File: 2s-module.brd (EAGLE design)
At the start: 19.4 x 48.2 mm, 36 parts, among them J1 CQ-USB-C16PSMT01, Q1 IRFR9020A, U1 MCP4725, U2 PC817XI, U3 LM393DR, U4 MICROCHIP_MIC5219-3_3YM5-TRMI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

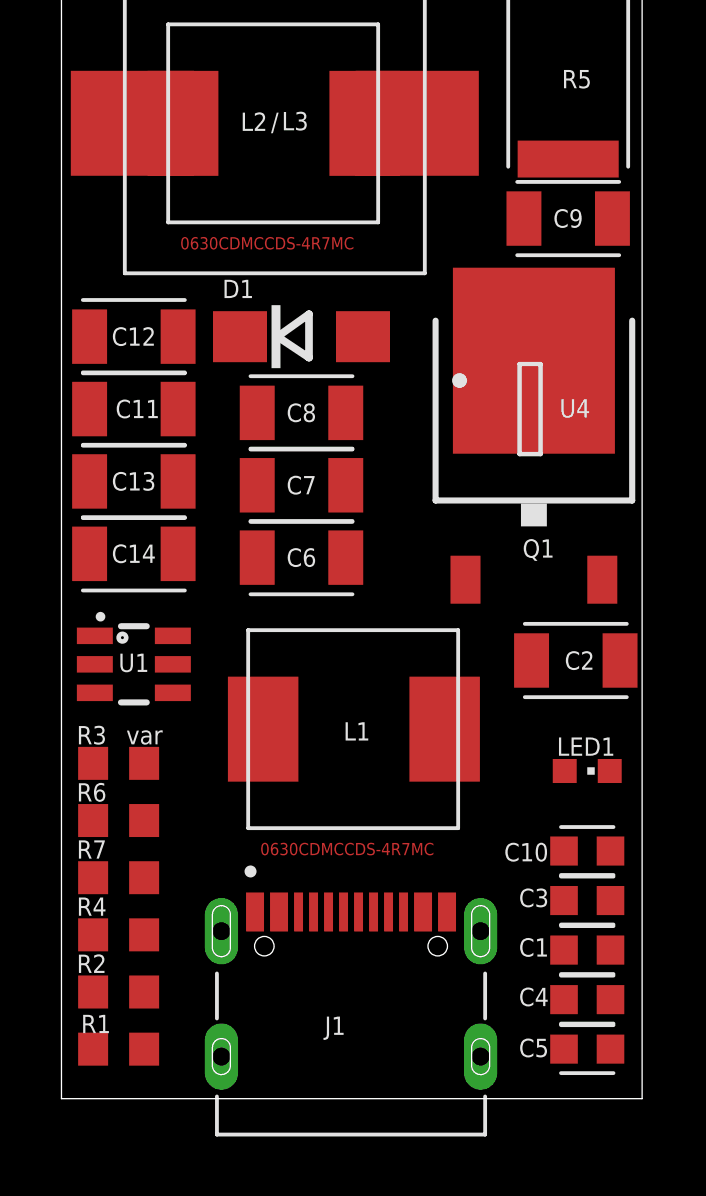
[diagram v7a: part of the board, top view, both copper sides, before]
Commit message: move buried component
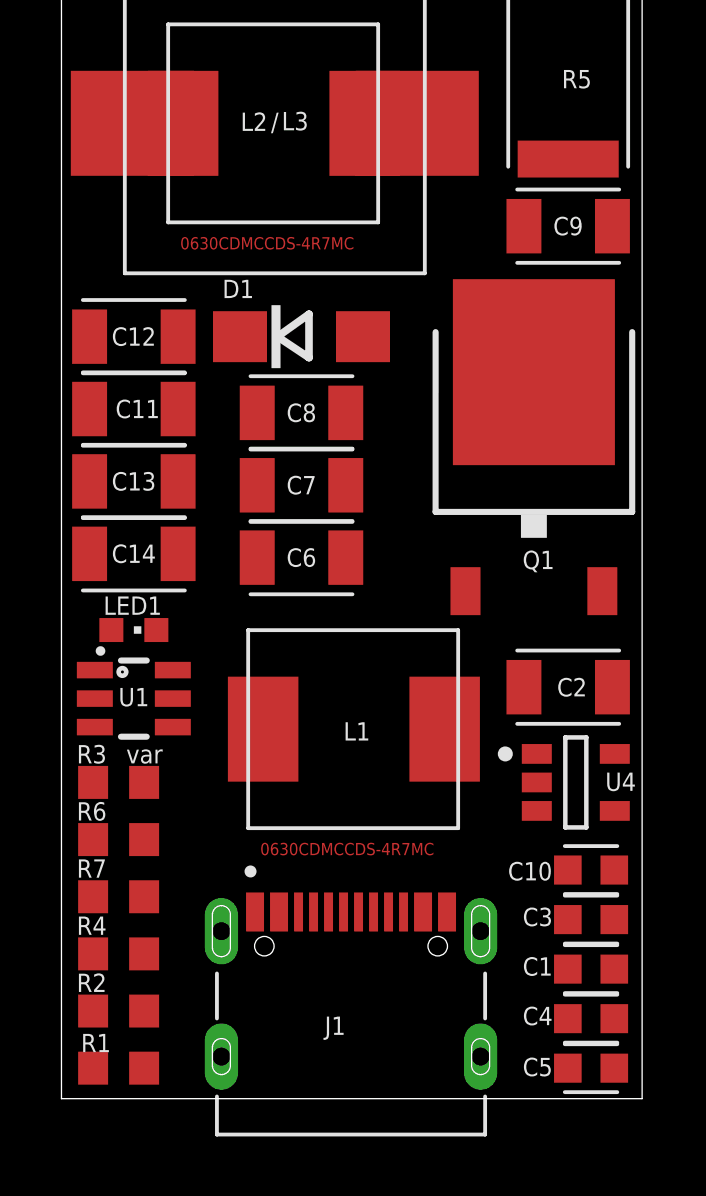
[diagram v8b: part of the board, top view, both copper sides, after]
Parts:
- moved LED1 15.8 mm to (2.67, 15.6)
- moved U4 12.5 mm to (17.4, 10.5)
- moved U1 1.14 mm to (2.67, 13.3)
- moved C2 0.92 mm to (17.1, 13.7)
- moved C1 0.65 mm to (17.9, 4.32)
- moved C10 0.65 mm to (17.9, 7.62)
- moved C4 0.65 mm to (17.9, 2.67)
- moved C5 0.65 mm to (17.9, 1.02)
- moved C3 0.65 mm to (17.9, 5.97)
- moved R6 0.64 mm to (2.16, 8.64)
- moved R4 0.64 mm to (2.16, 4.83)
- moved R2 0.64 mm to (2.16, 2.92)
- moved R1 0.64 mm to (2.16, 1.02)
- moved R3 0.63 mm to (2.16, 10.5)
- moved R7 0.63 mm to (2.16, 6.73)
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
